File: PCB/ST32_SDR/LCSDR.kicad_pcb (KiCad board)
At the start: 2 copper layers, 100 x 95.9 mm, 267 parts, among them CON1 +13,8v, IC1 ATMEGA328-A, J2 LINE OUT, K1 LU-12, P1 BNC, P10 CONN_01X01, P11 CONN_01X01, P12 CONN_01X01, P13 CONN_01X01, P2 SPI, P3 USB_OTG, P4 PA_TX, P5 ENCODER, Q1 IRF510N, Q2 MMBT2222LT1G, Q3 BFG135, Q4 PMBT2907, Q5 PMBT2222, Q6 PMBT2222, T1 1:4, T2 1_9, U1 MC33179DR2G, U10 74LVC1G3157, U11 SN74LVC1G00DCKR, U12 PE4259ds, U13 LD1117v33, U14 74HC4053, U15 L78M09, U16 FT232RL, U17 ADuM1201BR, U18 Si570, U19 PE4259ds, U2 PE4259ds, U20 PE4259ds, U21 PE4259ds, U22 PE4259ds, U23 PE4259ds, U24 PE4259ds, U25 PE4259ds, U26 PE4259ds, U27 LM78L06ACZ, U28 MC34063, U3 74LVC1G3157, U4 PE4259ds, U5 LD1117v25, U6 74HC4053, U7 SN74LVC1G00DCKR, U8 MC33179DR2G, U9 74LCX574, Y5 12Mhz

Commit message: Schematics update
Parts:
- removed C2: 10uF, LCSDR:Universal_C_Radial_D5_L11_P2_tantal
- removed C5: 100nF, LCSDR:C_1206_0603
- removed C8, C9: 10uF, Capacitors_Tantalum_SMD:CP_Tantalum_Case-A_EIA-3216-18_Hand
- removed J2: LINE OUT, LCSDR:audio_jack_3_5mm_PJ307
- removed L3: 47uH, LCSDR:Resistor_Horizontal_RM10mm
- removed R13, R20: 47R, LCSDR:R_1206_0603
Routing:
- net Net-(C74-Pad1): track 181.2 -> 140.9 mm, vias 2 -> 1
- net Net-(C76-Pad1): track 188.9 -> 152.0 mm
- net Net-(J2-Pad2): track 11.1 -> 0.00 mm
- net Net-(J2-Pad4): track 9.05 -> 0.00 mm
- net Net-(C9-Pad2): track 8.92 -> 0.00 mm
- net Net-(C2-Pad1): track 24.7 -> 15.9 mm
- net Net-(C8-Pad2): track 8.30 -> 0.00 mm
- net Net-(C8-Pad1): track 3.90 -> 0.00 mm
- net Net-(C9-Pad1): track 3.63 -> 0.00 mm
- net Net-(R20-Pad2): track 6.07 -> 3.22 mm
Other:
- board text removed: "LINE IN"
- board text removed: "LINE OUT"

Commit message: update schematics
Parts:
- removed C1: 10uF, LCSDR:Universal_C_Radial_D5_L11_P2_tantal
- removed C76: 100nF, LCSDR:C_1206_0603
- removed C77: 100uF, LCSDR:C_Radial_D5_L11_P2.5
- removed U15: L78M09, TO_SOT_Packages_SMD:TO-252-2_Rectifier
- removed U6: 74HC4053, Housings_SOIC:SOIC-16_3.9x9.9mm_Pitch1.27mm
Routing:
- net Net-(C76-Pad1): track 152.0 -> 96.4 mm
- net GND: track 1129.6 -> 1124.8 mm, vias 296 -> 292
- net Net-(C1-Pad1): track 87.8 -> 83.3 mm

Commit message: begin PCB
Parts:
- removed C10, C100, C101, C102, C103, C21, C24, C54, C67, C81, C91: 1uF, LCSDR:C_1206_0603
- removed C104, C105, C106, C107, C108, C110, C111, C56, C86, C93: 15nF, Capacitors_SMD:C_0603_HandSoldering
- removed C109: 15n, Capacitors_SMD:C_0603_HandSoldering
- removed C11: 22pF, LCSDR:C_1206_0603
- removed C16, C18, C22, C31, C47, C53, C6, C68, C70, C72, C73, C74, C78, C82, C87, C89, C94, C96: 100nF, LCSDR:C_1206_0603
- removed C20, C83, C92: 100uF, LCSDR:C_Radial_D5_L11_P2.5
- removed C23, C51: 27nF, LCSDR:C_1206_0603
- removed C48, C80: 10uF 16v, Capacitors_Tantalum_SMD:CP_Tantalum_Case-A_EIA-3216-18_Hand
- removed C52: 10uF, Capacitors_Tantalum_SMD:CP_Tantalum_Case-A_EIA-3216-18_Hand
- removed C55, C98, C99: 1000uF, Capacitors_ThroughHole:CP_Radial_D8.0mm_P3.50mm
- removed C57, C97: 180pF, Capacitors_SMD:C_0603_HandSoldering
- removed C58, C66: 6.8uF, Capacitors_Tantalum_SMD:CP_Tantalum_Case-A_EIA-3216-18_Hand
- removed C59, C64: 10n, LCSDR:C_1206_0603
- removed C60, C69: 390p, Capacitors_SMD:C_0603_HandSoldering
- removed C61, C65: 360pF, Capacitors_SMD:C_0603_HandSoldering
- removed C62, C63: 33pF, Capacitors_SMD:C_0603_HandSoldering
- removed C71: 1n, LCSDR:C_1206_0603
- removed C75: 330uF, LCSDR:C_Radial_D10_L13_P5
- removed C79, C95: 10uF, LCSDR:Universal_C_Radial_D5_L11_P2_tantal
- removed C84, C85, C88, C90: 4.7uF, Capacitors_SMD:C_0603_HandSoldering
- removed CON1: +13,8v, LCSDR:BARREL_JACK
- removed D11: LED, LEDs:LED_D5.0mm
- removed D12: WE-TVS824011, TO_SOT_Packages_SMD:SOT-23-5_HandSoldering
- removed IC1: ATMEGA328-A, Housings_QFP:TQFP-32_7x7mm_Pitch0.8mm
- removed L10, L22, L25, L4, L5: 47uH, LCSDR:Resistor_Horizontal_RM10mm
- removed L11: 4.7uH, Resistors_SMD:R_1210_HandSoldering
- removed L12, L13: 472K, LCSDR:Resistor_Horizontal_RM10mm
- removed L14, L15, L16: 2.2uH, Resistors_SMD:R_1210_HandSoldering
- removed L17, L18, L19: 1uH, Resistors_SMD:R_1210_HandSoldering
- removed L20, L21, L7: 470nH, Resistors_SMD:R_1210_HandSoldering
- removed L23: 0.47uH, Resistors_SMD:R_1210_HandSoldering
- removed L24, L26, L6: 100uH, LCSDR:Resistor_Horizontal_RM10mm
- removed L27: 33uH, LCSDR:Choke_CD75
- removed L8, L9: 220nH, Resistors_SMD:R_1210_HandSoldering
- removed P1: BNC, LCSDR:BNC_Socket_TYCO-AMP
- removed P10, P11, P12, P13: CONN_01X01, Mounting_Holes:MountingHole_3.2mm_M3_ISO7380_Pad
- removed P2: SPI, Pin_Headers:Pin_Header_Straight_2x03_Pitch2.54mm
- removed P3: USB_OTG, Connect:USB_Mini-B
- removed P4: PA_TX, Pin_Headers:Pin_Header_Straight_1x02_Pitch2.54mm
- removed P5: ENCODER, Pin_Headers:Pin_Header_Straight_1x04_Pitch2.54mm
- removed Q1: IRF510N, LCSDR:TO-220_Horizontal_Reversed
- removed Q2: MMBT2222LT1G, TO_SOT_Packages_SMD:SOT-23_Handsoldering
- removed Q3: BFG135, LCSDR:SOT-223
- removed Q4: PMBT2907, TO_SOT_Packages_SMD:SOT-23_Handsoldering
- removed Q5, Q6: PMBT2222, TO_SOT_Packages_SMD:SOT-23_Handsoldering
- removed R22, R25, R39, R45, R5: 1k 1%, Resistors_SMD:R_0603_HandSoldering
- removed R23: 270R 1%, Resistors_SMD:R_0603_HandSoldering
- removed R24, R33, R36: 20R, LCSDR:R_1206_0603
- removed R26, R27: 3k 1%, Resistors_SMD:R_0603_HandSoldering
- removed R28, R29, R30, R35, R6: 10k, LCSDR:R_1206_0603
- removed R31: 82R, LCSDR:R_1206_0603
- removed R32: 33R, Resistors_SMD:R_2512_HandSoldering
- removed R34, R58, R59: k91, LCSDR:R_1206_0603
- removed R37, R54: 13R, LCSDR:R_1206_0603
- removed R38: 20, Resistors_SMD:R_0603_HandSoldering
- removed R40, R42, R43, R46, R47: 4.7k 1%, Resistors_SMD:R_0603_HandSoldering
- removed R41: 51, Resistors_SMD:R_0603_HandSoldering
- removed R44, R49: 15, Resistors_SMD:R_0603_HandSoldering
- removed R48: 4k75, Resistors_SMD:R_0603_HandSoldering
- removed R50, R65: 10k, Resistors_SMD:R_0603_HandSoldering
- removed R52, R53: 82, Resistors_SMD:R_0603_HandSoldering
- removed R56: 33R, LCSDR:R_1206_0603
- removed R57: 5R1, LCSDR:R_1206_0603
- removed R60: k56, LCSDR:R_1206_0603
- removed R61, R64: 2.2k, Resistors_ThroughHole:R_Axial_DIN0204_L3.6mm_D1.6mm_P2.54mm_Vertical
- removed R62, R70: 1k, LCSDR:R_1206_0603
- removed R63: k510, LCSDR:R_1206_0603
- removed R66: 1k, Resistors_SMD:R_0603_HandSoldering
- removed R67: 1k5, LCSDR:R_1206_0603
- removed R68, R69: 2k2, LCSDR:R_1206_0603
- removed R71, R74: 1R, Resistors_SMD:R_0603_HandSoldering
- removed R72: 4.7k, LCSDR:R_1206_0603
- removed R73: 330, LCSDR:R_1206_0603
- removed RV1: 5k, Potentiometers:Potentiometer_Trimmer_Bourns_3296W
- removed T1: 1:4, LCSDR:TRANSF1_4
- removed T2: 1_9, LCSDR:HF1_9
- removed U10: 74LVC1G3157, TO_SOT_Packages_SMD:SOT-23-6_Handsoldering
- removed U11: SN74LVC1G00DCKR, TO_SOT_Packages_SMD:SOT-353_SC-70-5_Handsoldering
- removed U12, U19, U21, U22, U23, U24, U25, U26: PE4259ds, TO_SOT_Packages_SMD:SOT-363_SC-70-6_Handsoldering
- removed U13: LD1117v33, LCSDR:SOT-223
- removed U14: 74HC4053, Housings_SOIC:SOIC-16_3.9x9.9mm_Pitch1.27mm
- removed U17: ADuM1201BR, Housings_SOIC:SOIC-8_3.9x4.9mm_Pitch1.27mm
- removed U18: Si570, Oscillators:Oscillator_SMD_SI570_SI571_HandSoldering
- removed U27: LM78L06ACZ, TO_SOT_Packages_THT:TO-92_Inline_Wide
- removed U28: MC34063, Housings_SOIC:SOIC-8_3.9x4.9mm_Pitch1.27mm
- removed U8: MC33179DR2G, LCSDR:SOIC-14_3.9x8.7mm_Pitch1.27mm
- removed U9: 74LCX574, Housings_SSOP:SSOP-20_5.3x7.2mm_Pitch0.65mm
- removed Y5: 12Mhz, Crystals:Crystal_HC49-U_Vertical
- added C1, C2: 100nF, UI:C_1206_0603, F.Cu at (201.4, 87.2)
- added C116: 10uF, Capacitors_ThroughHole:CP_Radial_D5.0mm_P2.00mm, F.Cu at (205.5, 87.2)
- added C8, C9: 470nF, UI:C_1206_0603, F.Cu at (201.4, 87.2)
- added D3: SS14, Diodes_SMD:D_SMA_Handsoldering, F.Cu at (231.9, 74.5)
- added J1: MIC_PTT, UI:audio_jack_3_5mm_PJ307, B.Cu at (211.1, 73.3)
- added J3: Audio-Jack-3_2Switches, UI:audio_jack_3_5mm_PJ307, B.Cu at (211.1, 86.2)
- added J4: LINEIN, UI:audio_jack_3_5mm_PJ307, B.Cu at (211.1, 112.3)
- added J5: USB_B_Mini, Connect:USB_Mini-B, B.Cu at (209.6, 125.4)
- added L3: 15uH, Choke_Axial_ThroughHole:Choke_Horizontal_RM10mm, F.Cu at (201.4, 87.2)
- added Q7: BC817, TO_SOT_Packages_SMD:SOT-23, F.Cu at (201.4, 87.2)
- added R13: 11k, UI:R_1206_0603, F.Cu at (201.4, 87.2)
- added R20: 680, UI:R_1206_0603, F.Cu at (139.6, 145.5)
- added R78: 100, UI:R_1206_0603, B.Cu at (142.0, 107.4)
- added R79: 100, UI:R_1206_0603, B.Cu at (139.4, 107.4)
- added RN1: 56R, Resistors_SMD:R_Array_Convex_4x0603, B.Cu at (118.8, 72.2)
- added RN2, RN9: 4.7k, Resistors_SMD:R_Array_Convex_4x0603, F.Cu at (201.4, 87.2)
- added RN3, RN8: 47, Resistors_SMD:R_Array_Convex_4x0603, F.Cu at (201.4, 87.2)
- added RN4: 47, Resistors_SMD:R_Array_Convex_4x0603, B.Cu at (133.6, 82.2)
- added RN5: 47, Resistors_SMD:R_Array_Convex_4x0603, B.Cu at (157.8, 111.8)
- added RN7: 47, Resistors_SMD:R_Array_Convex_4x0603, B.Cu at (165.2, 80.0)
- added U15: Nokia_5110_LCD, UI:Nokia_5110-3310_LCD, F.Cu at (94.3, 60.3)
- added U6: MC34063, UI:SOIC-8_3.9x4.9mm_Pitch1.27mm, F.Cu at (201.4, 87.2)
- added Y1: 20Mhz, Crystals:Crystal_HC49-U_Vertical, B.Cu at (117.6, 93.1)
- added Y2: Crystal, Crystals:Crystal_HC49-U_Vertical, F.Cu at (201.4, 87.2)
- C12: value 22pF -> 470nF; footprint LCSDR:C_1206_0603 -> UI:C_1206_0603; moved to B.Cu
- C13: value 10uF -> 470nF; footprint Capacitors_Tantalum_SMD:CP_Tantalum_Case-A_EIA-3216-18_Hand -> UI:C_1206_0603; moved to B.Cu
- C14, C15: value 100nF -> 1uF; footprint LCSDR:C_1206_0603 -> Capacitors_ThroughHole:CP_Radial_D4.0mm_P2.00mm; moved to B.Cu
- C17: value 10uF -> 1uF; footprint LCSDR:Universal_C_Radial_D5_L11_P2_tantal -> Capacitors_ThroughHole:CP_Radial_D4.0mm_P2.00mm
- C19: value 10uF 16v -> 1uF; footprint Capacitors_Tantalum_SMD:CP_Tantalum_Case-A_EIA-3216-18_Hand -> Capacitors_ThroughHole:CP_Radial_D4.0mm_P2.00mm; moved to B.Cu
- C25: value 1uF -> 330uF; footprint LCSDR:C_1206_0603 -> Capacitors_ThroughHole:CP_Radial_D10.0mm_P5.00mm; moved to F.Cu
- C26: value 120pF -> 100nF; footprint Capacitors_SMD:C_0603_HandSoldering -> UI:C_1206_0603
- C27: value 270pF -> 100nF; footprint LCSDR:C_1206_0603 -> UI:C_1206_0603
- C28: value 270pF -> 22; footprint LCSDR:C_1206_0603 -> UI:C_1206_0603; moved to B.Cu
- C29, C3: footprint LCSDR:C_1206_0603 -> UI:C_1206_0603
- C30: value 10uF 16v -> 22; footprint Capacitors_Tantalum_SMD:CP_Tantalum_Case-A_EIA-3216-18_Hand -> UI:C_1206_0603; moved to B.Cu
- C32: value 680pF -> 100nF; footprint Capacitors_SMD:C_0603_HandSoldering -> UI:C_1206_0603
- C33: value 27nF -> 100nF; footprint LCSDR:C_1206_0603 -> UI:C_1206_0603; moved to B.Cu
- C34: value 15nF -> 100nF; footprint Capacitors_SMD:C_0603_HandSoldering -> UI:C_1206_0603; moved to B.Cu
- C35: footprint LCSDR:C_1206_0603 -> UI:C_1206_0603; moved to B.Cu
- C36: value 680pF -> 10uF; footprint Capacitors_SMD:C_0603_HandSoldering -> Capacitors_ThroughHole:CP_Radial_D4.0mm_P2.00mm
- C37: value 820pF -> 10uF; footprint Capacitors_SMD:C_0603_HandSoldering -> Capacitors_ThroughHole:CP_Radial_D4.0mm_P2.00mm
- C38: value 820pF -> 1000uF; footprint Capacitors_SMD:C_0603_HandSoldering -> Capacitors_ThroughHole:CP_Radial_D10.0mm_P5.00mm
- C39: value 680pF -> 1000uF; footprint Capacitors_SMD:C_0603_HandSoldering -> Capacitors_ThroughHole:CP_Radial_D10.0mm_P5.00mm
- C4, C46: value 10uF -> 100nF; footprint LCSDR:Universal_C_Radial_D5_L11_P2_tantal -> UI:C_1206_0603; moved to F.Cu
- C40: value 1uF -> 200pF; footprint LCSDR:C_1206_0603 -> UI:C_1206_0603
- C41: value 10uF 16v -> 360pF; footprint Capacitors_Tantalum_SMD:CP_Tantalum_Case-A_EIA-3216-18_Hand -> UI:C_1206_0603
- C42: value 47uF -> 1000uF; footprint Capacitors_SMD:CP_Elec_6.3x7.7 -> Capacitors_ThroughHole:CP_Radial_D10.0mm_P5.00mm; moved to F.Cu
- C43: value 27nF -> 1000uF; footprint LCSDR:C_1206_0603 -> Capacitors_ThroughHole:CP_Radial_D10.0mm_P5.00mm
- C44: value 360pF -> 100nF; footprint Capacitors_SMD:C_0603_HandSoldering -> UI:C_1206_0603
- C45: value 820pF -> 100nF; footprint Capacitors_SMD:C_0603_HandSoldering -> UI:C_1206_0603
- C49: value 820pF -> 1uF; footprint Capacitors_SMD:C_0603_HandSoldering -> Capacitors_ThroughHole:CP_Radial_D4.0mm_P2.00mm
- C50: value 33pF -> 220; footprint Capacitors_SMD:C_0603_HandSoldering -> UI:C_1206_0603
- C7: value 10uF -> 100nF; footprint Capacitors_Tantalum_SMD:CP_Tantalum_Case-A_EIA-3216-18_Hand -> UI:C_1206_0603
- D1: moved to B.Cu
- D2: value 1N5819 -> SS14; footprint Diodes_ThroughHole:D_DO-41_SOD81_P10.16mm_Horizontal -> Diodes_SMD:D_SMA_Handsoldering; moved to F.Cu
- K1: value LU-12 -> FRT5; footprint Relays_ThroughHole:Relay_SPDT_HJR-4102 -> Relays_ThroughHole:Relay_DPDT_FRT5
- L1: value 100uH -> 280uH; footprint LCSDR:Resistor_Horizontal_RM10mm -> Choke_Axial_ThroughHole:Choke_Horizontal_RM10mm; moved to F.Cu
- L2: value 4.7uH -> 19uH; footprint LCSDR:Choke_CD54 -> Choke_Axial_ThroughHole:Choke_Horizontal_RM10mm; moved to F.Cu
- R1, R2: value 3k 1% -> 100; footprint Resistors_SMD:R_0603_HandSoldering -> UI:R_1206_0603
- R10, R9: value 3k 1% -> 0.49R; footprint Resistors_SMD:R_0603_HandSoldering -> Resistors_ThroughHole:R_Axial_DIN0207_L6.3mm_D2.5mm_P10.16mm_Horizontal
- R11, R12: value 510R -> 0.49R; footprint LCSDR:R_1206_0603 -> Resistors_ThroughHole:R_Axial_DIN0207_L6.3mm_D2.5mm_P10.16mm_Horizontal
- R14: value 10k -> 1k; footprint Resistors_SMD:R_0603_HandSoldering -> UI:R_1206_0603
- R15: value 510R -> 18k; footprint LCSDR:R_1206_0603 -> UI:R_1206_0603
- R16: value 510R -> 6.2k; footprint LCSDR:R_1206_0603 -> UI:R_1206_0603
- R17: value 20R -> 33; footprint LCSDR:R_1206_0603 -> UI:R_1206_0603; moved to B.Cu
- R18: value 3k 1% -> 33; footprint Resistors_SMD:R_0603_HandSoldering -> UI:R_1206_0603; moved to B.Cu
- R19: value 10k -> 100; footprint LCSDR:R_1206_0603 -> UI:R_1206_0603; moved to B.Cu
- R21: value 3k 1% -> 56R; footprint Resistors_SMD:R_0603_HandSoldering -> UI:R_1206_0603
- R3: value 1k 1% -> 100; footprint Resistors_SMD:R_0603_HandSoldering -> UI:R_1206_0603
- R4: value 270R 1% -> 4.7k; footprint Resistors_SMD:R_0603_HandSoldering -> UI:R_1206_0603; moved to B.Cu
- R7, R8: value 1k -> 0*; footprint LCSDR:R_1206_0603 -> UI:R_1206_0603
- R75: value 11k -> 4.7k; footprint Resistors_ThroughHole:R_Axial_DIN0204_L3.6mm_D1.6mm_P2.54mm_Vertical -> UI:R_1206_0603; moved to F.Cu
- R76: value 18k -> 4.7k; footprint Resistors_ThroughHole:R_Axial_DIN0204_L3.6mm_D1.6mm_P2.54mm_Vertical -> UI:R_1206_0603; moved to F.Cu
- U1: value MC33179DR2G -> SI5351A; footprint Housings_SOIC:SOIC-14_3.9x8.7mm_Pitch1.27mm -> Housings_SSOP:MSOP-10_3x3mm_Pitch0.5mm
- U16: value FT232RL -> WM8731_alt; moved to B.Cu
- U2: value PE4259ds -> FM24CL16B; footprint TO_SOT_Packages_SMD:SOT-363_SC-70-6_Handsoldering -> Housings_SOIC:SOIC-8_3.9x4.9mm_Pitch1.27mm; moved to B.Cu
- U20: value PE4259ds -> 4066; footprint TO_SOT_Packages_SMD:SOT-363_SC-70-6_Handsoldering -> Housings_SOIC:SOIC-14_3.9x8.7mm_Pitch1.27mm; moved to B.Cu
- U3: value 74LVC1G3157 -> STM32F401RCTx; footprint TO_SOT_Packages_SMD:SOT-23-6_Handsoldering -> Housings_QFP:LQFP-64_10x10mm_Pitch0.5mm; moved to B.Cu
- U4: value PE4259ds -> AP1117-33; footprint TO_SOT_Packages_SMD:SOT-363_SC-70-6_Handsoldering -> TO_SOT_Packages_SMD:SOT-223
- U5: value LD1117v25 -> MC34063; footprint LCSDR:SOT-223 -> UI:SOIC-8_3.9x4.9mm_Pitch1.27mm
- U7: value SN74LVC1G00DCKR -> 78M09; footprint TO_SOT_Packages_SMD:SOT-353_SC-70-5_Handsoldering -> TO_SOT_Packages_SMD:TO-252-2_Rectifier
- moved C26 155.0 mm to (201.4, 87.2)
- moved U4 153.6 mm to (201.4, 87.2), turned to 90 degrees
- moved R75 153.2 mm to (205.5, 87.2)
- moved R76 152.2 mm to (205.5, 87.2)
- moved C46 151.6 mm to (205.5, 87.2), turned to 90 degrees
- moved R15 151.2 mm to (201.4, 87.2)
- moved C27 150.7 mm to (201.4, 87.2), turned to 90 degrees
- moved R16 149.8 mm to (201.4, 87.2)
- moved R17 147.1 mm to (201.5, 126.2), turned to 180 degrees
- moved C32 146.5 mm to (201.4, 87.2)
- moved C13 144.7 mm to (195.3, 97.5), turned to 180 degrees
- moved U20 143.9 mm to (195.4, 102.3), turned to 180 degrees
- moved C38 143.1 mm to (201.4, 87.2), turned to 90 degrees
- moved C39 142.8 mm to (201.4, 87.2), turned to 90 degrees
- moved D2 142.7 mm to (201.4, 87.2), turned to 90 degrees
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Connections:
- C12 pad 2: GND -> LINE_OUT_LEFT
- C13 pad 2: GND -> LINE_OUT_RIGHT
- C14 pad 1: Net-(C13-Pad1) -> LINE_IN_LEFT
- C14 pad 2: GND -> Net-(C14-Pad2)
- C15 pad 1: Net-(C15-Pad1) -> LINE_IN_RIGHT
- C17 pad 1: VDD -> Net-(C17-Pad1)
- C17 pad 2: GND -> Net-(C17-Pad2)
- C25 pad 1: GND -> +3V3
- C25 pad 2: Net-(C10-Pad2) -> GND
- C26 pad 1: Net-(C26-Pad1) -> +3V3
- C26 pad 2: Net-(C26-Pad2) -> GND
- C27 pad 1: GND -> +3V3
- C27 pad 2: Net-(C27-Pad2) -> GND
- C28 pad 1: GND -> Net-(C28-Pad1)
- C28 pad 2: Net-(C26-Pad2) -> GND
- C29 pad 1: Net-(C15-Pad1) -> MCU_RESET
- C29 pad 2: Net-(C15-Pad2) -> GND
- C3 pad 1: VDD -> CLK1
- C3 pad 2: GND -> Net-(C3-Pad2)
- C30 pad 2: Net-(C30-Pad2) -> GND
- C32 pad 2: Net-(C32-Pad2) -> GND
- C33 pad 1: Net-(C30-Pad2) -> GND
- C33 pad 2: GND -> +3V3
- C34 pad 2: Net-(C34-Pad2) -> +3V3
- C35 pad 1: Net-(C35-Pad1) -> GND
- C35 pad 2: Net-(C35-Pad2) -> +3V3
- C36 pad 1: GND -> +9V
- C36 pad 2: Net-(C36-Pad2) -> GND
- C37 pad 1: GND -> +12V
- C37 pad 2: Net-(C36-Pad2) -> GND
- C38 pad 1: GND -> +3V3
- C38 pad 2: Net-(C32-Pad2) -> GND
- C39 pad 1: GND -> +9V
- C39 pad 2: Net-(C32-Pad2) -> GND
- C4 pad 1: VDD -> CLK2
- C4 pad 2: GND -> Net-(C4-Pad2)
- C40 pad 1: GND -> Net-(C40-Pad1)
- C40 pad 2: Net-(C40-Pad2) -> GND
- C41 pad 2: Net-(C41-Pad2) -> GND
- C42 pad 1: Net-(C40-Pad2) -> +3V3
- C43 pad 1: Net-(C41-Pad2) -> +9V
- C44 pad 1: Net-(C44-Pad1) -> Net-(C116-Pad1)
- C44 pad 2: Net-(C44-Pad2) -> GND
- C45 pad 2: Net-(C45-Pad2) -> +3V3
- C46 pad 1: Net-(C46-Pad1) -> +3V3
- C49 pad 1: GND -> MIC_IN
- C49 pad 2: Net-(C44-Pad2) -> Net-(C49-Pad2)
- C50 pad 1: Net-(C44-Pad1) -> Net-(C49-Pad2)
- C50 pad 2: Net-(C44-Pad2) -> GND
- C7 pad 1: Net-(C1-Pad1) -> PTTIN
- D1 pad 1: Net-(C74-Pad1) -> Net-(D1-Pad1)
- D1 pad 2: Net-(C93-Pad2) -> PTTIN
- K1 pad 1: Net-(C15-Pad1) -> Net-(K1-Pad1)
- K1 pad 5: Net-(C74-Pad1) -> (no net)
- K1 pad 6: Net-(K1-Pad6) -> (no net)
- K1 pad 7: Net-(K1-Pad7) -> Net-(J4-Pad1)
- K1 pad 8: Net-(C93-Pad2) -> Net-(C15-Pad2)
- L1 pad 1: Net-(C76-Pad1) -> +3V3
- L1 pad 2: VDD -> +3V3
- L2 pad 1: Net-(C40-Pad2) -> Net-(D2-Pad1)
- L2 pad 2: Net-(C74-Pad1) -> +3V3
- R1 pad 1: /270_2 -> CLK0
- R1 pad 2: Net-(C1-Pad1) -> GND
- R10 pad 1: Net-(C1-Pad1) -> +12V
- R10 pad 2: /90_2 -> Net-(R10-Pad2)
- R11 pad 1: GND -> Net-(R11-Pad1)
- R11 pad 2: Net-(C1-Pad1) -> +9V
- R12 pad 1: Net-(C1-Pad1) -> Net-(R10-Pad2)
- R12 pad 2: Net-(C2-Pad1) -> +12V
- R14 pad 1: VDD -> Net-(R14-Pad1)
- R14 pad 2: Net-(C34-Pad2) -> GND
- R15 pad 1: Net-(C13-Pad1) -> +3V3
- R15 pad 2: GND -> Net-(R13-Pad1)
- R16 pad 1: /2,75V -> +9V
- R16 pad 2: Net-(C13-Pad1) -> Net-(R14-Pad1)
- R17 pad 1: /90_1 -> Net-(J5-Pad3)
- R17 pad 2: Net-(C19-Pad2) -> USB_DP
- R18 pad 1: /0_2 -> Net-(J5-Pad2)
- R18 pad 2: Net-(C1-Pad1) -> USB_DM
- R19 pad 1: Net-(Q2-Pad1) -> Net-(R19-Pad1)
- R19 pad 2: Net-(C110-Pad2) -> I2S_MCLK
- R2 pad 1: Net-(C1-Pad1) -> CLK1
- R2 pad 2: Net-(R2-Pad2) -> GND
- R21 pad 1: Net-(C1-Pad1) -> LCD_CLK
- R3 pad 1: Net-(R2-Pad2) -> CLK2
- R3 pad 2: Net-(R3-Pad2) -> GND
- R4 pad 1: Net-(R2-Pad2) -> +3V3
- R4 pad 2: Net-(R4-Pad2) -> PTTIN
- R7 pad 1: Net-(C46-Pad1) -> GND
- R7 pad 2: Net-(C71-Pad1) -> Net-(R7-Pad2)
- R75 pad 1: GND -> +3V3
- R76 pad 1: Net-(R75-Pad2) -> +3V3
- R76 pad 2: Net-(C10-Pad2) -> Net-(R76-Pad2)
- R8 pad 1: Net-(C71-Pad1) -> Net-(R8-Pad1)
- R9 pad 1: Net-(R4-Pad2) -> +9V
- R9 pad 2: Net-(R13-Pad2) -> Net-(R11-Pad1)
- U1 pad 1: Net-(R22-Pad2) -> +3V3
- U1 pad 10: /90_2 -> Net-(C2-Pad2)
- U1 pad 2: Net-(R21-Pad2) -> Net-(U1-Pad2)
- U1 pad 3: /0_2 -> Net-(U1-Pad3)
- U1 pad 4: Net-(C2-Pad1) -> I2C_SCL
- U1 pad 5: /180_2 -> I2C_SDA
- U1 pad 6: Net-(R23-Pad2) -> Net-(C4-Pad2)
- U1 pad 7: Net-(R20-Pad2) -> +3V3
- U1 pad 8: Net-(R13-Pad2) -> GND
- U1 pad 9: Net-(R4-Pad2) -> Net-(C3-Pad2)
- U16 pad 1: Net-(U16-Pad1) -> +3V3
- U16 pad 10: Net-(U16-Pad10) -> Net-(C19-Pad1)
- U16 pad 11: Net-(U16-Pad11) -> GND
- U16 pad 12: Net-(U16-Pad12) -> LINE_OUT_LEFT
- U16 pad 13: Net-(U16-Pad13) -> LINE_OUT_RIGHT
- U16 pad 14: Net-(U16-Pad14) -> +3V3
- U16 pad 15: Net-(D12-Pad3) -> GND
- U16 pad 16: Net-(D12-Pad4) -> Net-(C116-Pad1)
- U16 pad 17: Net-(C96-Pad1) -> MIC_BIAS
- U16 pad 18: Net-(C94-Pad2) -> MIC_IN
- U16 pad 19: Net-(R72-Pad2) -> LINE_IN_RIGHT
- U16 pad 20: Net-(C94-Pad1) -> LINE_IN_LEFT
- U16 pad 21: Net-(C94-Pad2) -> GND
- U16 pad 22: Net-(U16-Pad22) -> GND
- U16 pad 23: Net-(U16-Pad23) -> Net-(R76-Pad2)
- U16 pad 24: Net-(U16-Pad24) -> Net-(R75-Pad2)
- U16 pad 25: Net-(C94-Pad2) -> Net-(R19-Pad1)
- U16 pad 26: Net-(C94-Pad2) -> Net-(U16-Pad26)
- U16 pad 27: Net-(U16-Pad27) -> +3V3
- U16 pad 28: Net-(U16-Pad28) -> GND
- U16 pad 4: Net-(C94-Pad1) -> Net-(RN7-Pad2)
- U16 pad 5: Net-(U16-Pad5) -> Net-(RN7-Pad3)
- U16 pad 7: Net-(C94-Pad2) -> Net-(RN7-Pad3)
- U16 pad 8: Net-(U16-Pad8) -> +3V3
- U16 pad 9: Net-(U16-Pad9) -> Net-(C17-Pad1)
- U2 pad 2: GND -> Net-(U2-Pad2)
- U2 pad 3: Net-(K1-Pad7) -> Net-(U2-Pad3)
- U2 pad 4: Net-(U2-Pad4) -> GND
- U2 pad 5: Net-(U2-Pad5) -> I2C_SDA
- U2 pad 6: Net-(C10-Pad2) -> I2C_SCL
- U20 pad 1: Net-(C32-Pad2) -> Net-(C8-Pad2)
- U20 pad 2: GND -> Net-(C12-Pad1)
- U20 pad 3: Net-(U20-Pad3) -> Net-(C13-Pad1)
- U20 pad 5: Net-(C35-Pad1) -> Net-(RN4-Pad7)
- U20 pad 6: Net-(C10-Pad2) -> (no net)
- U3 pad 1: /270_1 -> Net-(U3-Pad1)
- U3 pad 2: GND -> KEY_B
- U3 pad 3: /90_1 -> KEY_C
- U3 pad 4: Net-(C35-Pad2) -> KEY_D
- U3 pad 5: Net-(C21-Pad1) -> Net-(C28-Pad1)
- U3 pad 6: /90 -> Net-(C30-Pad1)
- U4 pad 1: Net-(C27-Pad2) -> GND
- U4 pad 2: GND -> +3V3
- U4 pad 3: Net-(U4-Pad3) -> +12V
- U4 pad 4: Net-(C104-Pad2) -> (no net)
- U5 pad 1: Net-(R31-Pad1) -> Net-(R11-Pad1)
- U5 pad 2: /2,75V -> Net-(D2-Pad1)
- U5 pad 3: Net-(C76-Pad1) -> Net-(C40-Pad1)
- U5 pad 4: /2,75V -> GND
- U7 pad 1: Net-(U7-Pad1) -> +12V
- U7 pad 2: Net-(U7-Pad1) -> GND
- U7 pad 3: GND -> +9V
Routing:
- net GND: track 1124.8 -> 0.00 mm, vias 292 -> 0
- net Net-(C10-Pad2): track 276.2 -> 0.00 mm, vias 20 -> 0
- net Net-(IC1-Pad27): track 146.3 -> 0.00 mm, vias 5 -> 0
- net Net-(C74-Pad1): track 140.9 -> 0.00 mm, vias 1 -> 0
- net Net-(IC1-Pad28): track 139.0 -> 0.00 mm, vias 4 -> 0
- net Net-(C104-Pad2): track 114.5 -> 0.00 mm
- net Net-(C9-Pad2): track 102.8 -> 0.00 mm, vias 2 -> 0
- net Net-(C108-Pad2): track 98.0 -> 0.00 mm, vias 2 -> 0
- net Net-(C76-Pad1): track 96.4 -> 0.00 mm, vias 1 -> 0
- net Net-(C107-Pad2): track 89.6 -> 0.00 mm, vias 2 -> 0
- net Net-(C1-Pad1): track 83.3 -> 0.00 mm, vias 3 -> 0
- net Net-(K1-Pad7): track 82.4 -> 0.00 mm, vias 1 -> 0
- net Net-(C105-Pad2): track 78.3 -> 0.00 mm, vias 3 -> 0
- net Net-(IC1-Pad23): track 61.4 -> 0.00 mm
- net Net-(C94-Pad1): track 52.1 -> 0.00 mm, vias 1 -> 0
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- removed copper zone on B.Cu, net Net-(C94-Pad2)
- removed copper zone on F.Cu, net Net-(C94-Pad2)
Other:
- board size 100 x 95.9 mm -> 150 x 100 mm
- net class Default: trace_width 0.3 -> 0.2
- board text removed: "+13.8V"
- board text removed: "ANT"
- board text removed: "USB"

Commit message: PCB update
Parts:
- removed C12, C13, C9: 470nF, UI:C_1206_0603
- removed R78, R79: 100, UI:R_1206_0603
- removed RN4, RN5: 47, Resistors_SMD:R_Array_Convex_4x0603
- removed U20: 4066, Housings_SOIC:SOIC-14_3.9x8.7mm_Pitch1.27mm
- added C16: 100nF, UI:C_1206_0603, B.Cu at (194.2, 121.8)
- added C22: 100nF, UI:C_1206_0603, B.Cu at (155.2, 110.1)
- added C23: 100nF, UI:C_1206_0603, B.Cu at (143.8, 110.7)
- added C24: 100nF, UI:C_1206_0603, B.Cu at (150.5, 122.0)
- added C31: C_Small, UI:C_1206_0603, B.Cu at (78.2, 108.3)
- added C5: 100nF, UI:C_1206_0603, F.Cu at (139.7, 150.0)
- added C55: C_Small, UI:C_1206_0603, B.Cu at (90.2, 108.1)
- added C6: 100nF, UI:C_1206_0603, B.Cu at (197.3, 61.1)
- added C68: C_Small, UI:C_1206_0603, B.Cu at (101.4, 108.2)
- added C74: C_Small, UI:C_1206_0603, B.Cu at (112.0, 108.1)
- added D4: D_Small, Diodes_SMD:D_MiniMELF_Handsoldering, B.Cu at (190.2, 119.1)
- added D5: D_Small, Diodes_SMD:D_MiniMELF_Handsoldering, B.Cu at (197.3, 68.9)
- added J2: IDC10 Serial Wire, UI:USBBLASTER, B.Cu at (143.9, 45.1)
- added K2: FRT5, Relays_ThroughHole:Relay_DPDT_FRT5, B.Cu at (193.4, 72.7)
- added Q1: Q_NPN_BEC, TO_SOT_Packages_SMD:SOT-23_Handsoldering, B.Cu at (185.5, 119.6)
- added Q2: Q_NPN_BEC, TO_SOT_Packages_SMD:SOT-23_Handsoldering, B.Cu at (200.4, 67.7)
- added R5: 2.2k, UI:R_1206_0603, F.Cu at (133.7, 147.3)
- added R6: 2.2k, UI:R_1206_0603, B.Cu at (202.7, 73.2)
- added R97: 56R, UI:R_1206_0603, B.Cu at (101.4, 97.1)
- added R98: 56R, UI:R_1206_0603, F.Cu at (139.9, 138.6)
- added SW1: SW_Push_Dual, Buttons_Switches_ThroughHole:SW_PUSH_6mm_h13mm, F.Cu at (75.0, 105.5)
- added SW2: SW_Push_Dual, Buttons_Switches_ThroughHole:SW_PUSH_6mm_h13mm, F.Cu at (87.0, 105.8)
- added SW3: SW_Push_Dual, Buttons_Switches_ThroughHole:SW_PUSH_6mm_h13mm, F.Cu at (98.2, 105.7)
- added SW4: SW_Push_Dual, Buttons_Switches_ThroughHole:SW_PUSH_6mm_h13mm, F.Cu at (108.7, 105.5)
- added SW5: ENCODER, UI:SF-ROTARY-ENCODER, F.Cu at (146.9, 118.0)
- C1, C116, C2, C25, C26, C27, C29, C3, C32, C37, C38, C39, C4, C40, C41, C42, C43, C44, C45, C46, C7, D2, D3, Q7, R1, R10, R12, R13, R14, R15, R16, R2, R3, R7, R75, R76, R8, RN2, RN3, RN8, RN9, U1, U4, U5, U6, U7, Y2: moved to B.Cu
- C8: value 470nF -> 100nF; moved to B.Cu
- L2: footprint Choke_Axial_ThroughHole:Choke_Horizontal_RM10mm -> Choke_Toroid_ThroughHole:Choke_Toroid_5x10mm_Vertical
- L3: footprint Choke_Axial_ThroughHole:Choke_Horizontal_RM10mm -> Choke_Toroid_ThroughHole:Choke_Toroid_5x10mm_Vertical; moved to B.Cu
- moved D3 163.7 mm to (70.1, 49.7), turned to 180 degrees
- moved D2 136.9 mm to (70.1, 126.1), turned to 180 degrees
- moved C41 136.5 mm to (71.0, 46.7), turned to 180 degrees
- moved L3 136.4 mm to (67.4, 61.6)
- moved C40 134.5 mm to (71.5, 122.2), turned to 180 degrees
- moved R14 130.2 mm to (78.7, 43.4), turned to 180 degrees
- moved C27 129.9 mm to (72.2, 73.2)
- moved R15 128.8 mm to (79.2, 128.0)
- moved U6 128.5 mm to (79.2, 47.4), turned to 0 degrees
- moved U5 127.2 mm to (79.2, 122.8), turned to 0 degrees
- moved R16 126.9 mm to (79.2, 52.7)
- moved R13 126.6 mm to (78.7, 118.8), turned to 180 degrees
- moved C7 124.0 mm to (211.4, 44.4)
- moved R10 121.5 mm to (88.1, 43.3), turned to 270 degrees
- moved R12 121.2 mm to (84.9, 53.5)
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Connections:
- C7 pad 1: PTTIN -> PTT_IN
- C8 pad 1: I_OUT -> Net-(C8-Pad1)
- C8 pad 2: Net-(C8-Pad2) -> GND
- D1 pad 2: PTTIN -> PTT_IN
- K1 pad 1: Net-(K1-Pad1) -> +12V
- K1 pad 2: I_IN -> Q_IN
- K1 pad 4: Net-(J4-Pad2) -> Net-(J4-Pad1)
- K1 pad 7: Net-(J4-Pad1) -> Net-(J4-Pad2)
- K1 pad 9: Q_IN -> I_IN
- R4 pad 2: PTTIN -> PTT_IN
- R75 pad 2: Net-(R75-Pad2) -> I2C_SCL
- R76 pad 2: Net-(R76-Pad2) -> I2C_SDA
- RN2 pad 1: KEY_A -> KEY_D
- RN2 pad 2: KEY_B -> KEY_C
- RN2 pad 3: KEY_C -> KEY_B
- RN2 pad 4: KEY_D -> KEY_A
- RN3 pad 1: BAND0 -> BAND3
- RN3 pad 2: BAND1 -> BAND2
- RN3 pad 3: BAND2 -> BAND1
- RN3 pad 4: BAND3 -> BAND0
- RN7 pad 5: I2S_SDI -> I2S_SCLK
- RN7 pad 6: I2S_LRCK -> I2S_SDO
- RN7 pad 7: I2S_SDO -> I2S_LRCK
- RN7 pad 8: I2S_SCLK -> I2S_SDI
- RN9 pad 1: Net-(RN9-Pad1) -> KEY_MENU
- RN9 pad 2: ENCODER_B -> ENCODER_A
- RN9 pad 3: ENCODER_A -> ENCODER_B
- RN9 pad 4: KEY_MENU -> Net-(RN9-Pad4)
- RN9 pad 5: +3V3 -> Net-(RN9-Pad5)
- RN9 pad 8: Net-(RN9-Pad8) -> +3V3
- U16 pad 23: Net-(R76-Pad2) -> I2C_SDA
- U16 pad 24: Net-(R75-Pad2) -> I2C_SCL
- U16 pad 3: Net-(RN7-Pad1) -> Net-(RN7-Pad4)
- U16 pad 4: Net-(RN7-Pad2) -> Net-(RN7-Pad3)
- U16 pad 5: Net-(RN7-Pad3) -> Net-(RN7-Pad2)
- U16 pad 6: Net-(RN7-Pad4) -> Net-(RN7-Pad1)
- U16 pad 7: Net-(RN7-Pad3) -> Net-(RN7-Pad2)
- U3 pad 16: LINE_OUT_LEFT_MCU -> Net-(U3-Pad16)
- U3 pad 17: LINE_OUT_RIGHT_MCU -> Net-(U3-Pad17)
- U3 pad 61: I2C_SCL -> I2C_SCL_MCU
- U3 pad 62: I2C_SDA -> I2C_SDA_MCU
- U4 pad 3: +12V -> +9V
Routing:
- net +3V3: track 0.00 -> 9.89 mm
- net I2C_SCL: track 9.84 -> 0.00 mm
- net I2C_SDA: track 9.31 -> 0.00 mm
- net Net-(R7-Pad2): track 0.00 -> 9.05 mm
- net Net-(C32-Pad1): track 0.00 -> 8.35 mm

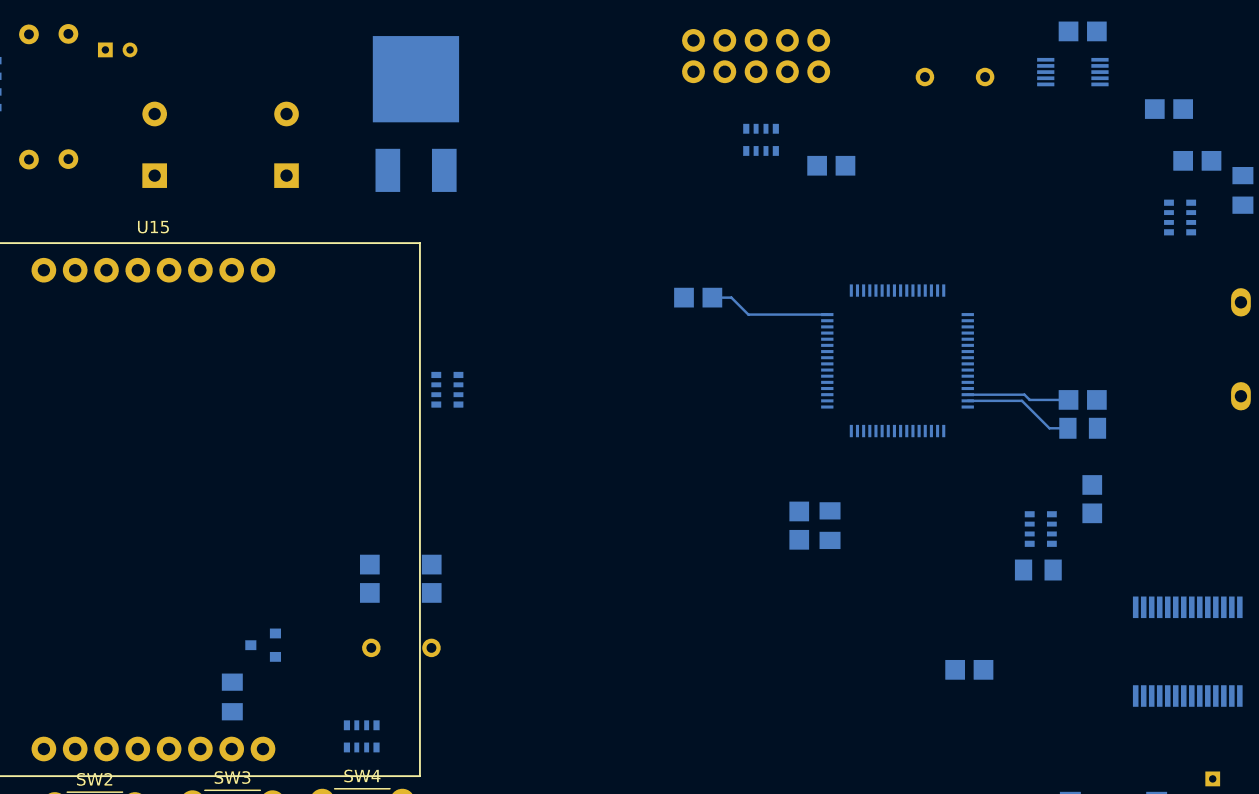
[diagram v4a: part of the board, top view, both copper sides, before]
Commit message: LCD at SPI3
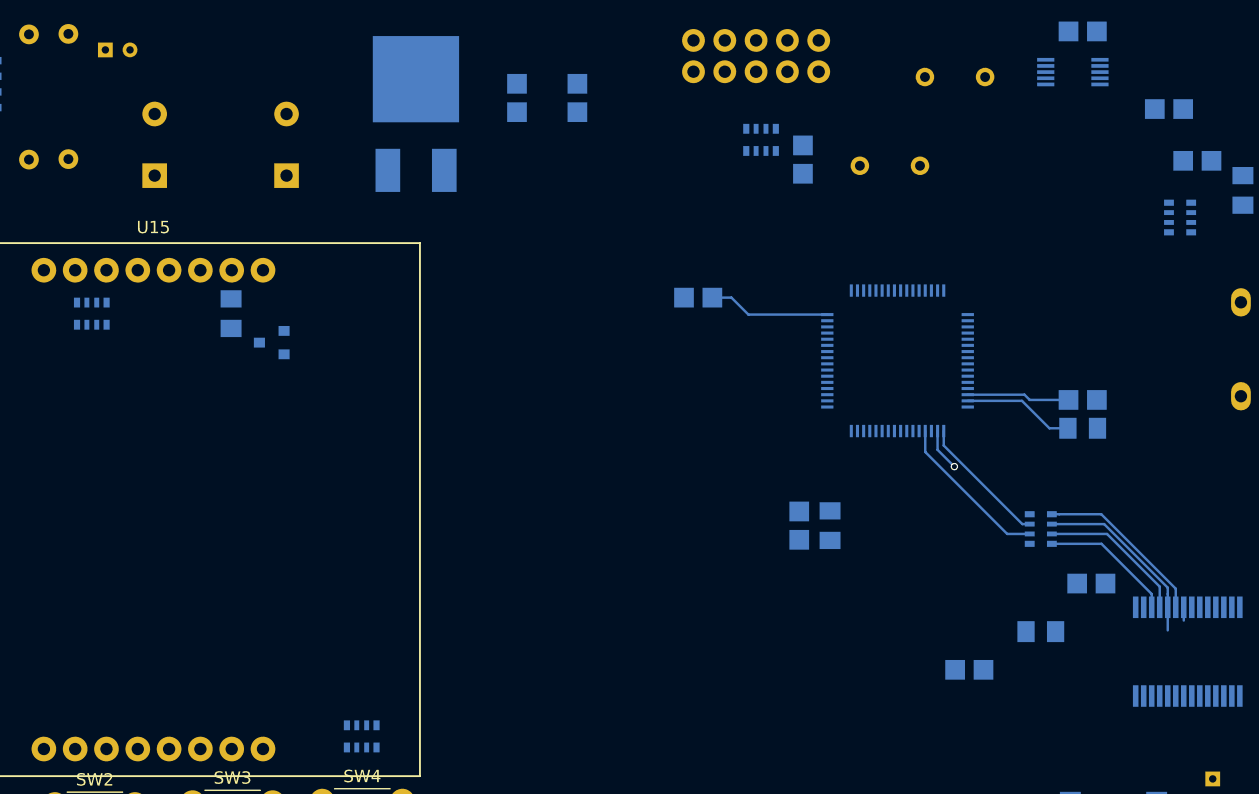
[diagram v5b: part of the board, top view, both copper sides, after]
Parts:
- moved Y1 52.3 mm to (152.3, 54.0), turned to 0 degrees
- moved C30 42.5 mm to (129.4, 48.5)
- moved C28 39.6 mm to (124.5, 48.5)
- moved R97 31.1 mm to (101.3, 66.0), turned to 270 degrees
- moved RN1 29.5 mm to (90.0, 66.0), turned to 270 degrees
- moved Q7 24.6 mm to (104.6, 68.3)
- moved C45 6.85 mm to (171.1, 87.9), turned to 0 degrees
- moved R19 5.00 mm to (167.0, 91.8)
- moved C29 2.35 mm to (147.7, 53.5), turned to 90 degrees
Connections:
- RN1 pad 1: LCD_RESET -> Net-(RN1-Pad1)
- RN1 pad 2: LCD_CE -> Net-(RN1-Pad2)
- RN1 pad 3: LCD_DC -> Net-(RN1-Pad3)
- RN1 pad 4: LCD_DIN -> Net-(RN1-Pad4)
- RN1 pad 5: Net-(RN1-Pad5) -> LCD_DIN
- RN1 pad 6: Net-(RN1-Pad6) -> LCD_DC
- RN1 pad 7: Net-(RN1-Pad7) -> LCD_CE
- RN1 pad 8: Net-(RN1-Pad8) -> LCD_RESET
- U15 pad 1: Net-(RN1-Pad8) -> Net-(RN1-Pad1)
- U15 pad 2: Net-(RN1-Pad7) -> Net-(RN1-Pad2)
- U15 pad 3: Net-(RN1-Pad6) -> Net-(RN1-Pad3)
- U15 pad 4: Net-(RN1-Pad5) -> Net-(RN1-Pad4)
- U3 pad 20: LCD_CE -> Net-(U3-Pad20)
- U3 pad 21: LCD_CLK -> Net-(U3-Pad21)
- U3 pad 22: LCD_DC -> Net-(U3-Pad22)
- U3 pad 23: LCD_DIN -> Net-(U3-Pad23)
- U3 pad 50: TX2 -> LCD_CE
- U3 pad 51: PTT_IN -> LCD_CLK
- U3 pad 52: KEY_CW -> LCD_DC
- U3 pad 53: KEY_A -> LCD_DIN
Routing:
- net Net-(RN7-Pad2): track 0.00 -> 16.1 mm
- net Net-(RN7-Pad1): track 0.00 -> 14.1 mm
- net I2S_SDO: track 0.00 -> 12.9 mm
- net Net-(RN7-Pad3): track 0.00 -> 12.2 mm
- net Net-(RN7-Pad4): track 0.00 -> 10.9 mm
- net I2S_LRCK: track 0.00 -> 10.8 mm
- net I2S_SCLK: track 0.00 -> 3.45 mm, vias 0 -> 1

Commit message: UI PCB linux 1
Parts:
- removed C31, C55, C68, C74: C_Small, UI:C_1206_0603
- removed R97, R98: 56R, UI:R_1206_0603
- added C10, C11, C12, C13, C9: 100nF, UI:C_1206_0603, F.Cu at (0.00, 0.00)
- added C18: 1nF, UI:C_1206_0603, B.Cu at (200.9, 76.5)
- added C20: 1nF, UI:C_1206_0603, F.Cu at (140.0, 145.1)
- added J10: Conn_01x01, Mounting_Holes:MountingHole_3.2mm_M3_DIN965_Pad, F.Cu at (70.0, 105.0)
- added J11: Conn_01x01, Mounting_Holes:MountingHole_3.2mm_M3_DIN965_Pad, F.Cu at (210.0, 105.0)
- added J6: IQ, Pin_Headers:Pin_Header_Straight_1x06_Pitch2.54mm, B.Cu at (196.4, 125.6)
- added J7: CLK, Pin_Headers:Pin_Header_Straight_1x06_Pitch2.54mm, B.Cu at (144.8, 125.6)
- added J8: Conn_01x01, Mounting_Holes:MountingHole_3.2mm_M3_DIN965_Pad, F.Cu at (210.0, 70.0)
- added J9: Conn_01x01, Mounting_Holes:MountingHole_3.2mm_M3_DIN965_Pad, F.Cu at (70.0, 70.0)
- added R22: 56, UI:R_1206_0603, B.Cu at (165.4, 102.0)
- added R23: 56, UI:R_1206_0603, B.Cu at (165.0, 99.2)
- added R24: 56R, UI:R_1206_0603, B.Cu at (103.0, 67.0)
- added R25: 56R, UI:R_1206_0603, F.Cu at (0.00, 0.00)
- added SW6: SW_Push_Dual, Buttons_Switches_ThroughHole:SW_PUSH_6mm_h13mm, F.Cu at (113.2, 105.7)
- C36, C49, C50, L2, R11, R20, R21, R9: moved to B.Cu
- K1, K2: footprint Relays_ThroughHole:Relay_DPDT_FRT5 -> UI:Relay_G6K-2F
- Q7: footprint TO_SOT_Packages_SMD:SOT-23 -> TO_SOT_Packages_SMD:SOT-23_Handsoldering
- moved L2 164.2 mm to (67.8, 131.6)
- moved R11 158.2 mm to (85.3, 123.5)
- moved C36 151.9 mm to (91.5, 114.6), turned to 0 degrees
- moved R9 143.8 mm to (88.5, 113.3), turned to 270 degrees
- moved L1 130.8 mm to (123.0, 112.0)
- moved C49 99.8 mm to (210.4, 65.0), turned to 90 degrees
- moved C50 99.7 mm to (203.7, 64.2), turned to 270 degrees
- moved R20 97.9 mm to (206.5, 64.2), turned to 270 degrees
- moved R21 84.7 mm to (96.6, 65.7), turned to 90 degrees
- moved U1 74.9 mm to (132.2, 111.2), turned to 270 degrees
- moved C25 59.3 mm to (74.0, 91.5), turned to 180 degrees
- moved Y2 56.9 mm to (131.8, 97.5), turned to 270 degrees
- moved C26 39.2 mm to (125.0, 103.0), turned to 90 degrees
- moved C27 35.9 mm to (104.4, 89.3)
- moved C19 33.5 mm to (200.0, 86.0)
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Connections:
- J2 pad 7: Net-(J2-Pad7) -> (no net)
- J2 pad 8: Net-(J2-Pad8) -> (no net)
- J3 pad 4: Net-(J3-Pad4) -> (no net)
- J3 pad 5: Net-(J3-Pad5) -> (no net)
- J5 pad 1: Net-(J5-Pad1) -> (no net)
- J5 pad 4: Net-(J5-Pad4) -> (no net)
- K2 pad 2: Net-(K2-Pad2) -> (no net)
- K2 pad 4: Q_OUT -> (no net)
- K2 pad 7: I_OUT -> (no net)
- R5 pad 2: TX2 -> (no net)
- RN3 pad 5: Net-(RN3-Pad5) -> (no net)
- RN3 pad 6: Net-(RN3-Pad6) -> (no net)
- RN3 pad 7: Net-(RN3-Pad7) -> (no net)
- RN3 pad 8: Net-(RN3-Pad8) -> (no net)
- RN9 pad 2: ENCODER_A -> ENCODER_B
- RN9 pad 3: ENCODER_B -> ENCODER_A
- RN9 pad 4: Net-(RN9-Pad4) -> KEY_E
- RN9 pad 5: Net-(RN9-Pad5) -> +3V3
- U16 pad 12: LINE_OUT_LEFT -> (no net)
- U16 pad 2: Net-(U16-Pad2) -> (no net)
- U16 pad 26: Net-(U16-Pad26) -> (no net)
- U2 pad 1: Net-(U2-Pad1) -> (no net)
- U2 pad 2: Net-(U2-Pad2) -> (no net)
- U2 pad 3: Net-(U2-Pad3) -> (no net)
- U3 pad 1: Net-(U3-Pad1) -> (no net)
- U3 pad 10: Net-(U3-Pad10) -> (no net)
- U3 pad 11: Net-(U3-Pad11) -> (no net)
- U3 pad 13: Net-(U3-Pad13) -> (no net)
- U3 pad 16: Net-(U3-Pad16) -> (no net)
- U3 pad 17: Net-(U3-Pad17) -> (no net)
- U3 pad 20: Net-(U3-Pad20) -> (no net)
- U3 pad 21: Net-(U3-Pad21) -> (no net)
- U3 pad 22: Net-(U3-Pad22) -> (no net)
- U3 pad 23: Net-(U3-Pad23) -> (no net)
- U3 pad 38: Net-(U3-Pad38) -> (no net)
- U3 pad 39: Net-(U3-Pad39) -> (no net)
- U3 pad 42: UART_RX -> (no net)
- U3 pad 43: UART_TX -> (no net)
- U3 pad 54: Net-(U3-Pad54) -> (no net)
- U3 pad 56: I_IN_M1 -> (no net)
- U3 pad 57: I_IN_M2 -> (no net)
- U3 pad 58: Q_IN_M1 -> (no net)
- U3 pad 59: Q_IN_M2 -> (no net)
- U3 pad 8: S-metr -> (no net)
- U3 pad 9: Net-(U3-Pad9) -> (no net)
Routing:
- net LCD_CE: track 0.00 -> 63.6 mm
- net LCD_DC: track 0.00 -> 62.1 mm
- net LCD_DIN: track 0.00 -> 61.0 mm
- net LCD_CLK: track 0.00 -> 59.0 mm, vias 0 -> 2
- net SWDIO: track 0.00 -> 35.7 mm, vias 0 -> 2
- net I2S_SDI: track 0.00 -> 26.8 mm
- net SWCLK: track 0.00 -> 26.8 mm, vias 0 -> 2
- net Net-(C30-Pad1): track 0.00 -> 22.1 mm
- net I2S_MCLK: track 0.00 -> 22.1 mm
- net SWO: track 0.00 -> 21.9 mm
- net I2S_SCLK: track 3.45 -> 22.5 mm, vias 1 -> 2
- net Net-(C28-Pad1): track 0.00 -> 17.9 mm
- net Net-(RN7-Pad2): track 16.1 -> 3.53 mm
- net I2S_LRCK: track 10.8 -> 23.1 mm
- net I2S_SDO: track 12.9 -> 23.8 mm
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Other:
- board size 150 x 100 mm -> 150 x 95 mm
- net class Default: trace_width 0.2 -> 0.25
